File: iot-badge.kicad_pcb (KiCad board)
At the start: 2 copper layers, 70 x 100 mm, 52 parts, among them J1 USB_C_Receptacle_USB2.0, J2 Wire ANT, Q1 BC847, Q2 BC847, SW1 SW_Push, SW2 SW_Push, SW3 SW_Push, SW4 SW_Push, SW5 SW_Push, SW6 SW_Push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

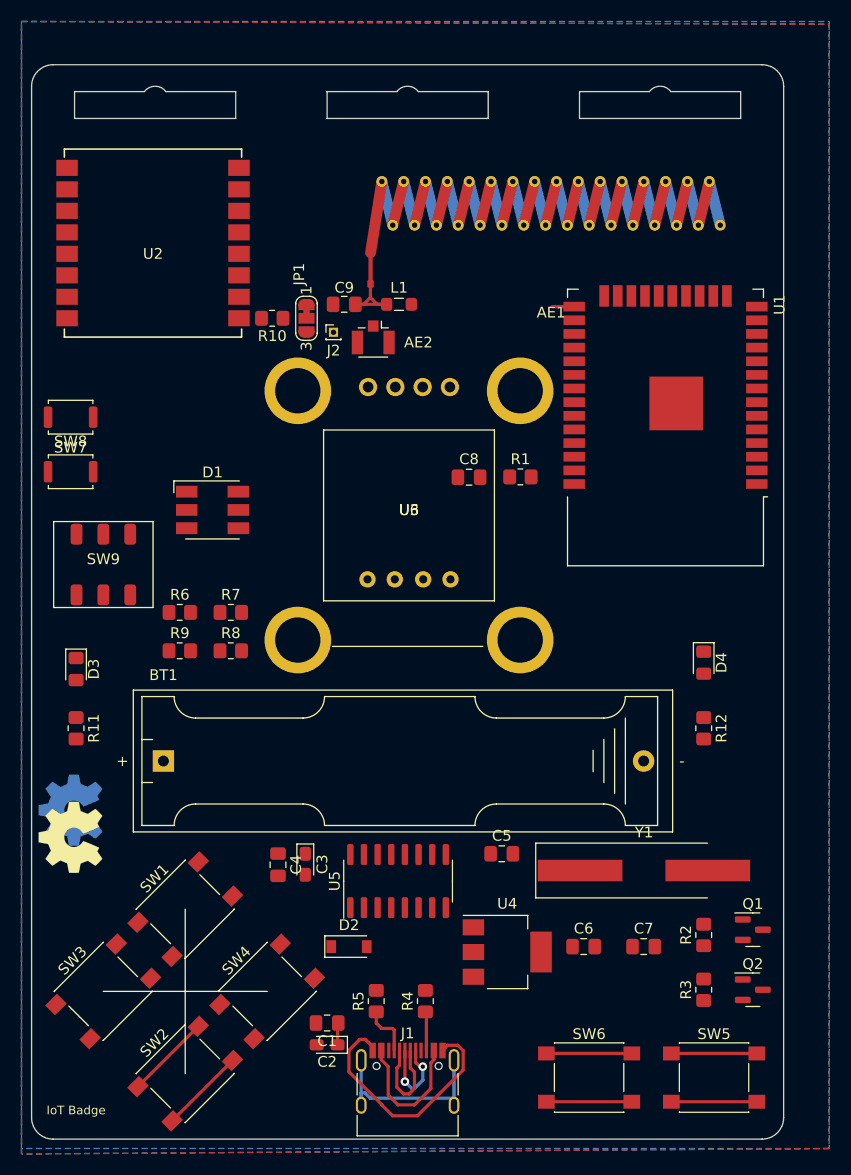
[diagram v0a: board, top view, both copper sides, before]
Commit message: all elements placed and wired
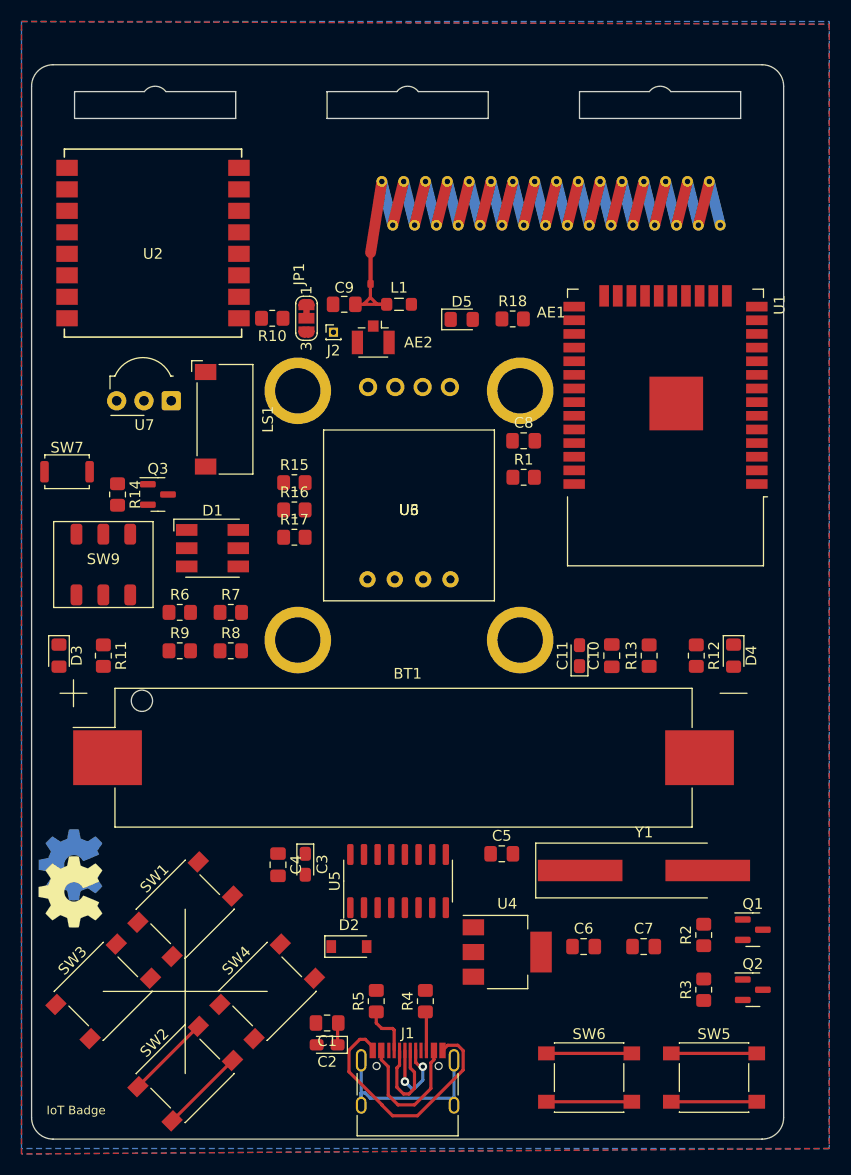
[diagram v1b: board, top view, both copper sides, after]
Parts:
- removed SW8: 0, Button_Switch_SMD:SW_Push_SPST_NO_Alps_SKRK
- added C10: 0.1uF, Capacitor_SMD:C_0805_2012Metric_Pad1.18x1.45mm_HandSolder, F.Cu at (154.0, 105.0)
- added C11: 100uF, Capacitor_Tantalum_SMD:CP_EIA-2012-15_AVX-P_Pad1.30x1.05mm_HandSolder, F.Cu at (151.0, 105.0)
- added D5: IRLED, LED_SMD:LED_0805_2012Metric_Pad1.15x1.40mm_HandSolder, F.Cu at (140.0, 73.7)
- added LS1: Speaker, Speaker_SMD:Speaker_SMD-10mmx5mm, F.Cu at (118.0, 83.0)
- added Q3: BC847, Package_TO_SOT_SMD:SOT-23, F.Cu at (111.8, 90.0)
- added R13: 220, Resistor_SMD:R_0805_2012Metric_Pad1.20x1.40mm_HandSolder, F.Cu at (157.5, 105.0)
- added R14: 2.2k, Resistor_SMD:R_0805_2012Metric_Pad1.20x1.40mm_HandSolder, F.Cu at (108.0, 90.0)
- added R15: 220, Resistor_SMD:R_0805_2012Metric_Pad1.20x1.40mm_HandSolder, F.Cu at (124.5, 88.9)
- added R16: 220, Resistor_SMD:R_0805_2012Metric_Pad1.20x1.40mm_HandSolder, F.Cu at (124.5, 91.4)
- added R17: 220, Resistor_SMD:R_0805_2012Metric_Pad1.20x1.40mm_HandSolder, F.Cu at (124.5, 94.0)
- added R18: 500, Resistor_SMD:R_0805_2012Metric_Pad1.20x1.40mm_HandSolder, F.Cu at (144.8, 73.7)
- added U7: TSOP41xx, OptoDevice:Vishay_MOLD-3Pin, F.Cu at (113.0, 81.3)
- BT1: footprint Battery:BatteryHolder_Keystone_2466_1xAAA -> Battery_SMD:BatteryHolder_Keystone_1020_1xAAA
- moved BT1 22.4 mm to (134.6, 114.5)
- moved R11 7.22 mm to (106.7, 105.0)
- moved R12 6.80 mm to (161.9, 105.0)
- moved C8 6.11 mm to (145.8, 85.0)
- moved SYMB1 5.08 mm to (103.6, 124.5)
- moved SYMB2 5.08 mm to (103.6, 127.0)
- moved D1 3.56 mm to (116.8, 95.0)
- moved D4 2.86 mm to (165.3, 105.0)
- moved D3 2.02 mm to (102.5, 105.0)
- moved SW7 0.33 mm to (103.3, 87.9)
- moved R1 0.31 mm to (145.8, 88.4)
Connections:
- D1 pad 1: unconnected-(D1-Pad1) -> Earth
- D1 pad 2: unconnected-(D1-Pad2) -> Earth
- D1 pad 3: unconnected-(D1-Pad3) -> Earth
- D1 pad 4: unconnected-(D1-Pad4) -> Net-(D1-Pad4)
- D1 pad 5: unconnected-(D1-Pad5) -> Net-(D1-Pad5)
- D1 pad 6: unconnected-(D1-Pad6) -> Net-(D1-Pad6)
- SW1 pad 1: unconnected-(SW1-Pad1) -> /SW1-0
- SW1 pad 2: unconnected-(SW1-Pad2) -> Earth
- SW2 pad 1: unconnected-(SW2-Pad1) -> /SW2-13
- SW2 pad 2: unconnected-(SW2-Pad2) -> Earth
- SW3 pad 1: unconnected-(SW3-Pad1) -> /SW3-16
- SW4 pad 1: unconnected-(SW4-Pad1) -> /SW4-17
- SW5 pad 1: unconnected-(SW5-Pad1) -> /SW5-32
- SW6 pad 1: unconnected-(SW6-Pad1) -> /SW6-33
- U1 pad 10: unconnected-(U1-Pad10) -> /DAC25
- U1 pad 14: unconnected-(U1-Pad14) -> /IRDEC12
- U1 pad 16: unconnected-(U1-Pad16) -> /SW2-13
- U1 pad 24: unconnected-(U1-Pad24) -> /IRLED2
- U1 pad 25: /IO0 -> /SW1-0
- U1 pad 27: unconnected-(U1-Pad27) -> /SW3-16
- U1 pad 28: unconnected-(U1-Pad28) -> /SW4-17
- U1 pad 33: unconnected-(U1-Pad33) -> /LEDG21
- U1 pad 36: unconnected-(U1-Pad36) -> /LEDG22
- U1 pad 37: unconnected-(U1-Pad37) -> /LEDB23
- U1 pad 8: unconnected-(U1-Pad8) -> /SW5-32
- U1 pad 9: unconnected-(U1-Pad9) -> /SW6-33
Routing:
- net unconnected-(SW2-Pad2): track 7.95 -> 0.00 mm
- net unconnected-(SW2-Pad1): track 7.95 -> 0.00 mm
- net /SW2-13: track 0.00 -> 7.95 mm
- net Earth: track 39.4 -> 47.4 mm
- net unconnected-(SW6-Pad1): track 7.95 -> 0.00 mm
- net unconnected-(SW5-Pad1): track 7.95 -> 0.00 mm
- net /SW6-33: track 0.00 -> 7.95 mm
- net /SW5-32: track 0.00 -> 7.95 mm
- net /IO0: track 2.09 -> 0.00 mm

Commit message: silk improvements
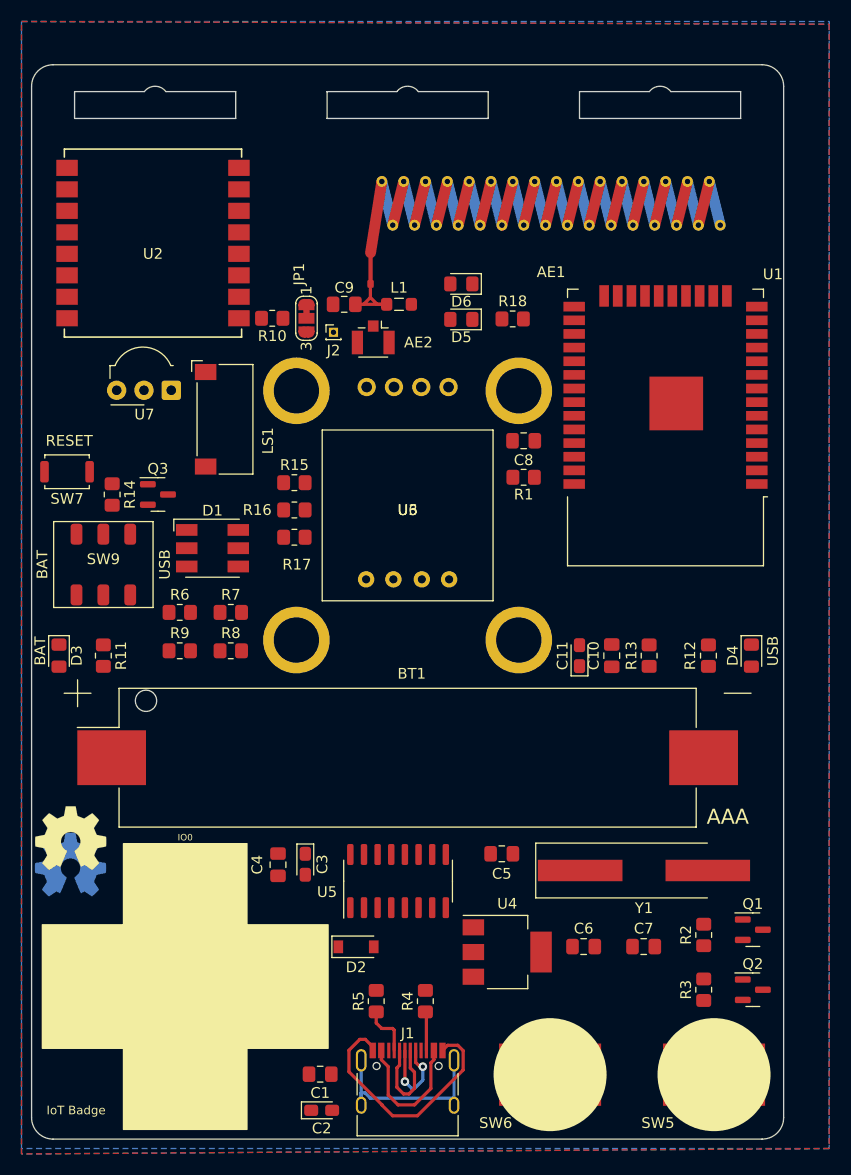
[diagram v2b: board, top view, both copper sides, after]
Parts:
- added D6: IRLED, LED_SMD:LED_0805_2012Metric_Pad1.15x1.40mm_HandSolder, F.Cu at (140.0, 70.4)
- moved C2 6.12 mm to (127.0, 147.3), turned to 0 degrees
- moved SYMB2 5.00 mm to (103.6, 122.0), turned to 0 degrees
- moved C1 4.81 mm to (126.9, 144.0), turned to 0 degrees
- moved SW6 3.64 mm to (148.3, 144.0)
- moved D4 1.66 mm to (167.0, 105.0)
- moved R12 1.13 mm to (163.0, 105.0)
- moved U7 0.98 mm to (113.0, 80.3)
- moved D2 0.66 mm to (130.2, 132.1)
- moved R14 0.50 mm to (107.5, 90.0)
- moved SW2 0.45 mm to (114.3, 143.4)
- moved SW1 0.45 mm to (114.3, 128.2)
- moved SW3 0.45 mm to (106.7, 135.8)
- moved SW4 0.45 mm to (121.9, 135.8)
- moved BT1 0.38 mm to (135.0, 114.5)
- moved SW5 0.27 mm to (163.5, 144.0)
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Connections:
- D5 pad 2: +3V3 -> Net-(D5-Pad2)
- Q2 pad 3: /IO0 -> /SW1-0
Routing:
- net /SW6-33: track 7.95 -> 0.00 mm
- net Earth: track 47.4 -> 39.4 mm
- net Net-(C1-Pad1): track 2.21 -> 0.00 mm
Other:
- board text added: "AAA"
- board text added: "BAT"
- board text added: "IO0"
- board text added: "RESET"
- board text added: "USB"

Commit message: all wired, unable to route
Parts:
- added R19: 0, Resistor_SMD:R_0805_2012Metric_Pad1.20x1.40mm_HandSolder, F.Cu at (139.0, 105.0)
- added R20: 0, Resistor_SMD:R_0805_2012Metric_Pad1.20x1.40mm_HandSolder, F.Cu at (137.0, 105.0)
- added R21: 0, Resistor_SMD:R_0805_2012Metric_Pad1.20x1.40mm_HandSolder, F.Cu at (106.7, 124.0)
- added R22: 0, Resistor_SMD:R_0805_2012Metric_Pad1.20x1.40mm_HandSolder, F.Cu at (101.8, 119.6)
- added R23: 0, Resistor_SMD:R_0805_2012Metric_Pad1.20x1.40mm_HandSolder, F.Cu at (103.8, 119.6)
- added R24: 0, Resistor_SMD:R_0805_2012Metric_Pad1.20x1.40mm_HandSolder, F.Cu at (104.7, 124.0)
- moved SYMB1 49.8 mm to (152.4, 114.3)
- moved SYMB2 37.5 mm to (109.2, 84.9)
- moved R13 23.5 mm to (134.0, 105.0)
- moved C10 22.0 mm to (132.0, 105.0)
- moved C11 21.0 mm to (130.0, 105.0)
- moved U7 5.00 mm to (108.0, 80.3)
- moved R18 4.54 mm to (143.2, 69.4)
- moved D5 4.36 mm to (139.3, 69.4)
- moved C8 4.20 mm to (145.8, 89.2), turned to 180 degrees
- moved R15 4.11 mm to (124.7, 93.0)
- moved R16 3.57 mm to (124.7, 95.0)
- moved R17 3.03 mm to (124.7, 97.0)
- moved R1 2.80 mm to (145.8, 91.2)
- moved R12 2.69 mm to (165.5, 106.0)
- moved SW7 2.42 mm to (103.3, 90.3)
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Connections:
- net /DAC25 renamed /DAC-25
- net /IRDEC12 renamed /IRDEC-12
- net /IRLED2 renamed /IRLED-2
- net /LEDB23 renamed /LEDB-23
- net /LEDG21 renamed /LEDR-21
- net /LEDG22 renamed /LEDG-22
- SW1 pad 1: /SW1-0 -> Net-(SW1-Pad1)
- SW2 pad 1: /SW2-13 -> Net-(SW2-Pad1)
- SW3 pad 1: /SW3-16 -> Net-(SW3-Pad1)
- SW4 pad 1: /SW4-17 -> Net-(SW4-Pad1)
- SW5 pad 1: /SW5-32 -> Net-(R19-Pad1)
- SW6 pad 1: /SW6-33 -> Net-(R20-Pad1)
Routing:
- net Earth: track 39.4 -> 23.5 mm, vias 0 -> 35
- net /SW2-13: track 7.95 -> 0.00 mm
- net /SW5-32: track 7.95 -> 0.00 mm
- net Net-(AE2-Pad1): track 0.00 -> 6.45 mm
- net Net-(C9-Pad2): track 0.00 -> 2.48 mm
- net Net-(JP1-Pad2): track 0.00 -> 2.19 mm
- net Net-(R10-Pad2): track 0.00 -> 2.10 mm
- net Net-(J1-PadA6): track 8.34 -> 10.1 mm
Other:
- board text added: "CE"
- board text added: "DISP_SSD1306"
- board text added: "GND"
- board text added: "IoT Badge V 00"
- board text added: "ME2188_PCB_MODULE"
- board text added: "SCL"
- board text added: "SDA"
- board text added: "VCC"
- board text added: "VOUT"
- board text removed: "IoT Badge"

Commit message: all wired, routed
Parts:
- removed R19, R20, R21, R22, R23, R24: 0, Resistor_SMD:R_0805_2012Metric_Pad1.20x1.40mm_HandSolder
- moved SW7 62.0 mm to (165.1, 95.3), turned to 90 degrees
- moved SW9 49.7 mm to (156.0, 103.0)
- moved R14 37.3 mm to (144.8, 90.0)
- moved LS1 37.2 mm to (153.0, 95.5), turned to 180 degrees
- moved Q3 33.9 mm to (145.3, 95.0), turned to -90 degrees
- moved R7 30.5 mm to (137.4, 77.0)
- moved R6 30.3 mm to (132.4, 77.0)
- moved D1 29.7 mm to (135.0, 71.5)
- moved L1 29.3 mm to (105.0, 71.9), turned to 180 degrees
- moved R15 28.5 mm to (140.6, 69.4)
- moved R16 28.4 mm to (140.6, 71.5)
- moved R17 28.3 mm to (140.6, 73.6)
- moved U2 25.5 mm to (112.0, 92.1), turned to 0 degrees
- moved AE1 25.4 mm to (122.9, 62.9)
- moved C10 25.4 mm to (152.4, 89.9)
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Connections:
- SW1 pad 1: Net-(SW1-Pad1) -> /SW1-0
- SW2 pad 1: Net-(SW2-Pad1) -> /SW2-13
- SW3 pad 1: Net-(SW3-Pad1) -> /SW3-16
- SW4 pad 1: Net-(SW4-Pad1) -> /SW4-17
- SW5 pad 1: Net-(R19-Pad1) -> /SW5-32
- SW6 pad 1: Net-(R20-Pad1) -> /SW6-33
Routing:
- net Earth: track 23.5 -> 200.6 mm, vias 35 -> 96
- net /SW1-0: track 0.00 -> 141.0 mm
- net /SW6-33: track 0.00 -> 139.9 mm, vias 0 -> 2
- net /SW5-32: track 0.00 -> 138.5 mm, vias 0 -> 4
- net +3.3VP: track 0.00 -> 132.5 mm
- net /SW2-13: track 0.00 -> 123.0 mm, vias 0 -> 2
- net +3V3: track 0.00 -> 115.2 mm, vias 0 -> 1
- net /SW3-16: track 0.00 -> 96.6 mm, vias 0 -> 2
- net /SW4-17: track 0.00 -> 94.8 mm, vias 0 -> 2
- net /EN: track 0.00 -> 73.7 mm, vias 0 -> 2
- net Net-(R8-Pad1): track 0.00 -> 69.8 mm, vias 0 -> 2
- net Net-(R9-Pad1): track 0.00 -> 69.5 mm
- net Net-(U1-Pad6): track 0.00 -> 59.2 mm, vias 0 -> 2
- net Net-(Q2-Pad2): track 0.00 -> 59.0 mm
- net Net-(R11-Pad2): track 0.00 -> 58.8 mm
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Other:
- outline, holes or cut-outs redrawn

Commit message: all wired, routed,fixes
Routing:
- net Earth: track 200.6 -> 199.7 mm
- net Net-(U1-Pad6): track 59.2 -> 58.7 mm

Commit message: finished pcb
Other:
- rule pad_to_mask_clearance: 0.051 -> 0
